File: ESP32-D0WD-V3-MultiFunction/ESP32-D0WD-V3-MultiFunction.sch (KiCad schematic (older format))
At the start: 7 parts

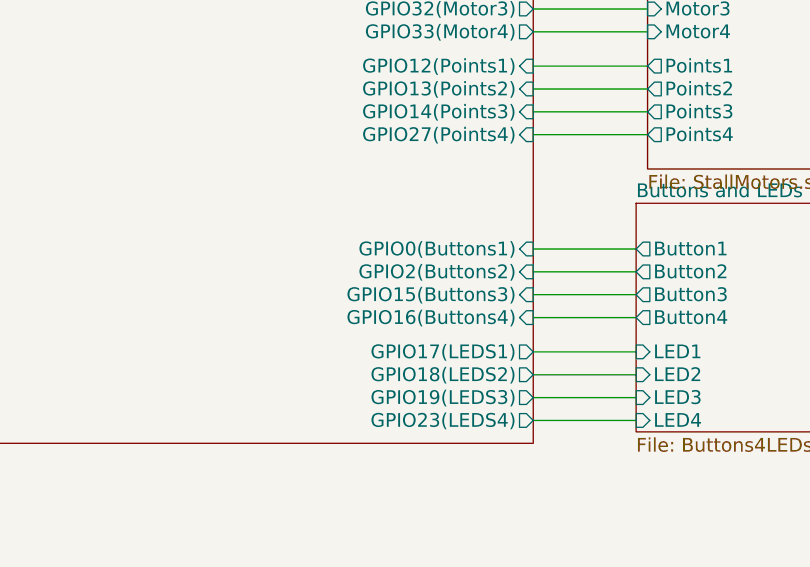
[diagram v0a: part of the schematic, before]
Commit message: Fix incorrect I/O pin assignments.
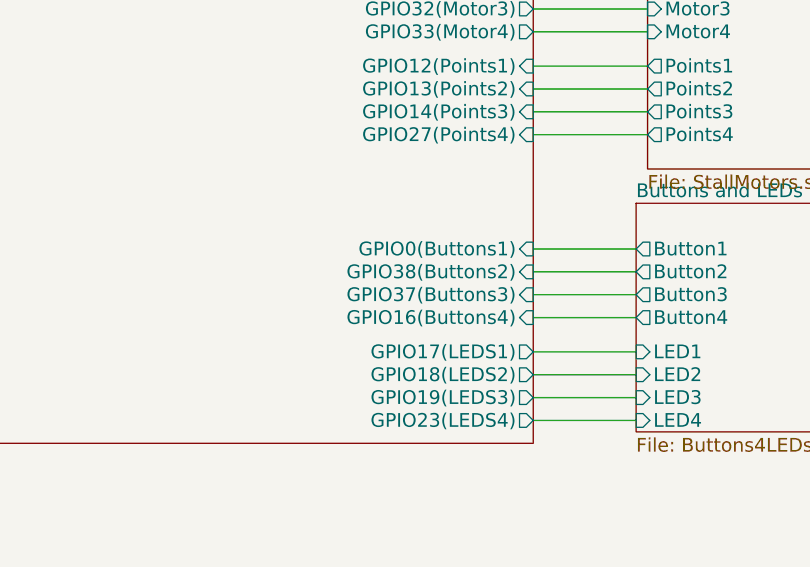
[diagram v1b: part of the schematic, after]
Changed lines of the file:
@@
 F10 "GPIO16(Buttons4)" I R 9000 3950 60
 F11 "GPIO0(Buttons1)" I R 9000 3650 60
-F12 "GPIO2(Buttons2)" I R 9000 3750 60
-F13 "GPIO27(Points4)" I R 9000 3150 60
-F14 "GPIO26(Motor2)" O R 9000 2500 60
-F15 "GPIO25(Motor1)" O R 9000 2400 60
-F16 "GPIO34(OD1)" I L 5150 3850 60
-F17 "GPIO35(OD2)" I L 5150 3950 60
-F18 "GPIO36(OD3)" I L 5150 4050 60
-F19 "GPIO39(OD4)" I L 5150 4150 60
-F20 "GPIO32(Motor3)" O R 9000 2600 60
-F21 "GPIO33(Motor4)" O R 9000 2700 60
-F22 "GPIO12(Points1)" I R 9000 2850 60
-F23 "GPIO13(Points2)" I R 9000 2950 60
-F24 "GPIO14(Points3)" I R 9000 3050 60
-F25 "GPIO15(Buttons3)" I R 9000 3850 60
+F12 "GPIO27(Points4)" I R 9000 3150 60
+F13 "GPIO26(Motor2)" O R 9000 2500 60
+F14 "GPIO25(Motor1)" O R 9000 2400 60
+F15 "GPIO34(OD1)" I L 5150 3850 60
+F16 "GPIO35(OD2)" I L 5150 3950 60
+F17 "GPIO36(OD3)" I L 5150 4050 60
+F18 "GPIO39(OD4)" I L 5150 4150 60
+F19 "GPIO32(Motor3)" O R 9000 2600 60
+F20 "GPIO33(Motor4)" O R 9000 2700 60
+F21 "GPIO12(Points1)" I R 9000 2850 60
+F22 "GPIO13(Points2)" I R 9000 2950 60
+F23 "GPIO14(Points3)" I R 9000 3050 60
+F24 "GPIO38(Buttons2)" I R 9000 3750 60
+F25 "GPIO37(Buttons3)" I R 9000 3850 60
 $EndSheet
 $Sheet
